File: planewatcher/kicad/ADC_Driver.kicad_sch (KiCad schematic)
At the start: 24 parts, among them U10 AD8138, U3 OPA2320

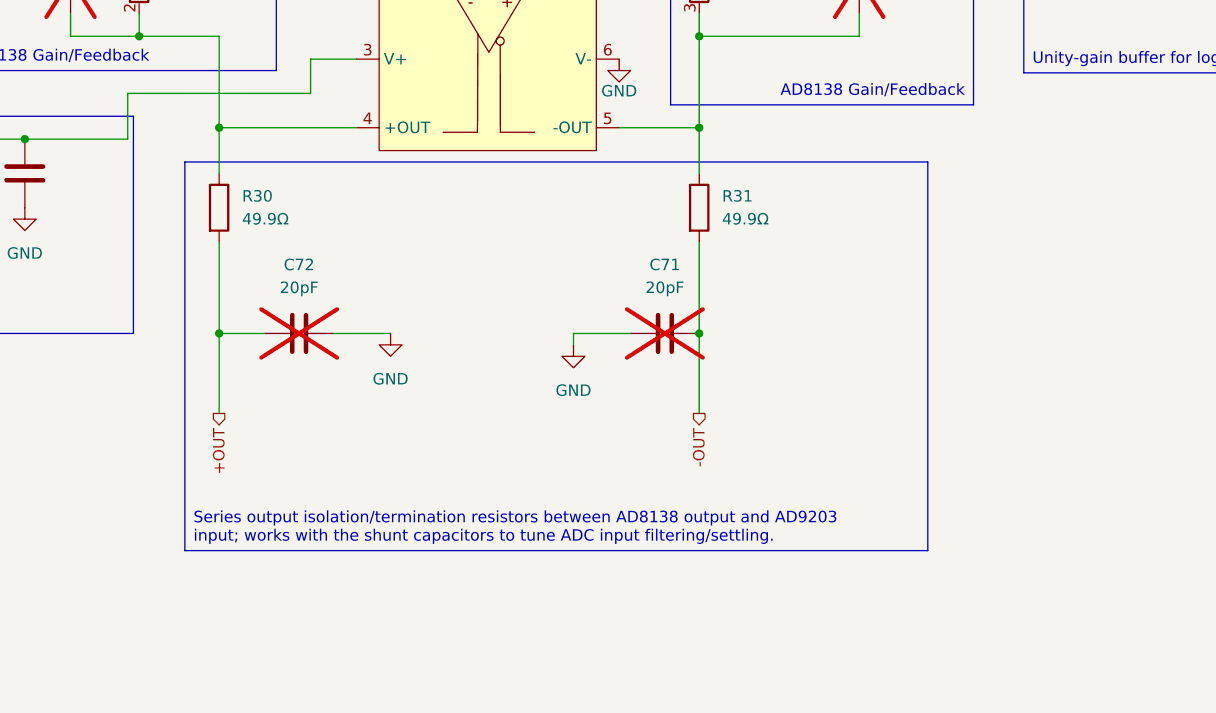
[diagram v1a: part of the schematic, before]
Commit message: Add RF pi matching networks + more
- Remove EEPROM write project solder jumper
- Update proto 1.3 documentation
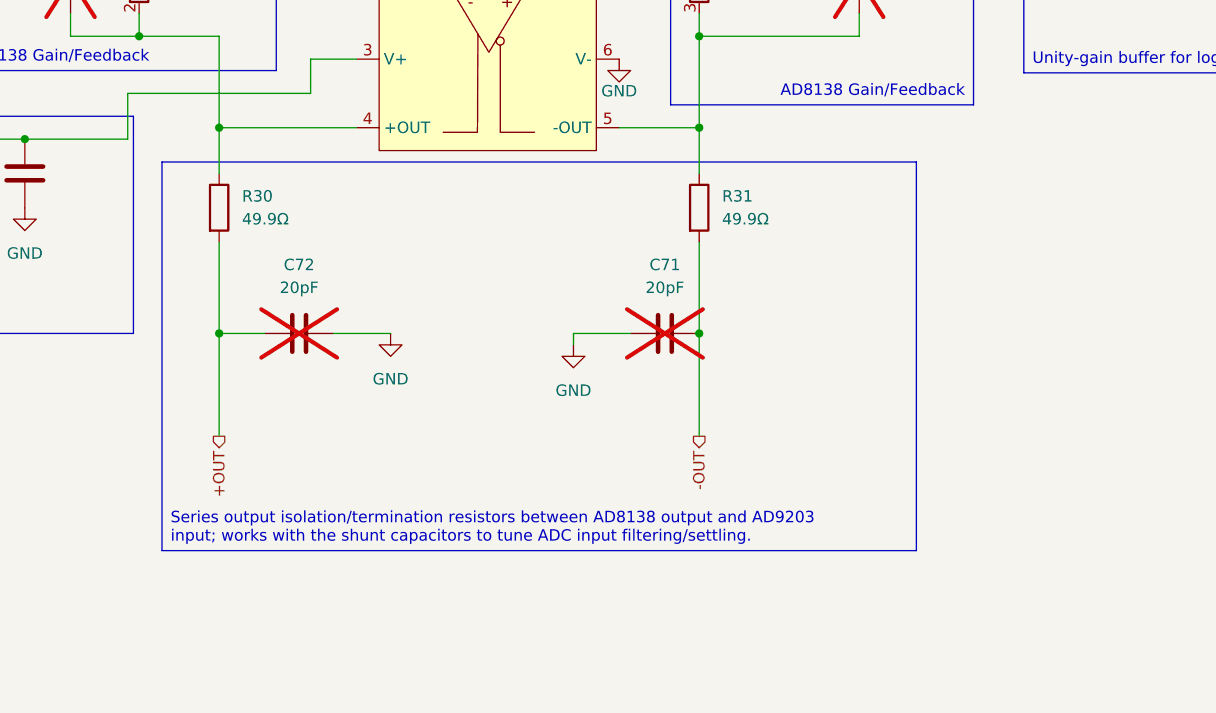
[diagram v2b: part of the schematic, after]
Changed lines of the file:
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@@
 	(text_box "Series output isolation/termination resistors between AD8138 output and AD9203 input; works with the shunt capacitors to tune ADC input filtering/settling."
 		(exclude_from_sim no)
-		(at 114.3 119.38 0)
-		(size 82.55 43.18)
+		(at 111.76 119.38 0)
+		(size 83.82 43.18)
 		(margins 0.9525 0.9525 0.9525 0.9525)
 		(stroke
@@
 	)
 	(junction
+		(at 109.22 105.41)
+		(diameter 0)
+		(color 0 0 0 0)
+	)
+	(junction
 		(at 118.11 138.43)
 		(diameter 0)
@@
 	)
 	(junction
-		(at 109.22 105.41)
+		(at 171.45 138.43)
 		(diameter 0)
 		(color 0 0 0 0)
@@
 	(junction
 		(at 220.98 74.93)
-		(diameter 0)
-		(color 0 0 0 0)
-	)
-	(junction
-		(at 171.45 138.43)
 		(diameter 0)
 		(color 0 0 0 0)
@@
 	(wire
 		(pts
-			(xy 171.45 138.43) (xy 171.45 147.32)
+			(xy 171.45 138.43) (xy 171.45 149.86)
 		)
 		(stroke
@@
 	(wire
 		(pts
-			(xy 118.11 138.43) (xy 118.11 147.32)
+			(xy 118.11 138.43) (xy 118.11 149.86)
 		)
 		(stroke
@@
 	(hierarchical_label "-OUT"
 		(shape output)
-		(at 171.45 147.32 270)
+		(at 171.45 149.86 270)
 		(effects
 			(font
@@
 	(hierarchical_label "+OUT"
 		(shape output)
-		(at 118.11 147.32 270)
+		(at 118.11 149.86 270)
 		(effects
 			(font
@@
 		)
 	)
+	(netclass_flag ""
+		(length 2.54)
+		(shape round)
+		(at 118.11 147.32 90)
+		(fields_autoplaced yes)
+		(effects
+			(font
+				(size 1.27 1.27)
+			)
+			(justify left bottom)
+		)
+		(property "Netclass" "DIFFPAIR_100Ω"
+			(at 115.57 146.6215 90)
+			(show_name no)
+			(do_not_autoplace no)
+			(effects
+				(font
+					(size 1.27 1.27)
+				)
+				(justify left)
+			)
+		)
+		(property "Component Class" ""
+			(at -85.09 10.16 0)
+			(show_name no)
+			(do_not_autoplace no)
+			(effects
+				(font
+					(size 1.27 1.27)
+					(italic yes)
+				)
+			)
+		)
+	)
+	(netclass_flag ""
+		(length 2.54)
+		(shape round)
+		(at 171.45 147.32 270)
+		(fields_autoplaced yes)
+		(effects
+			(font
+				(size 1.27 1.27)
+			)
+			(justify right bottom)
+		)
+		(property "Netclass" "DIFFPAIR_100Ω"
+			(at 173.99 146.6215 90)
+			(show_name no)
+			(do_not_autoplace no)
+			(effects
+				(font
+					(size 1.27 1.27)
+				)
+				(justify left)
+			)
+		)
+		(property "Component Class" ""
+			(at -31.75 10.16 0)
+			(show_name no)
+			(do_not_autoplace no)
+			(effects
+				(font
+					(size 1.27 1.27)
+					(italic yes)
+				)
+			)
+		)
+	)

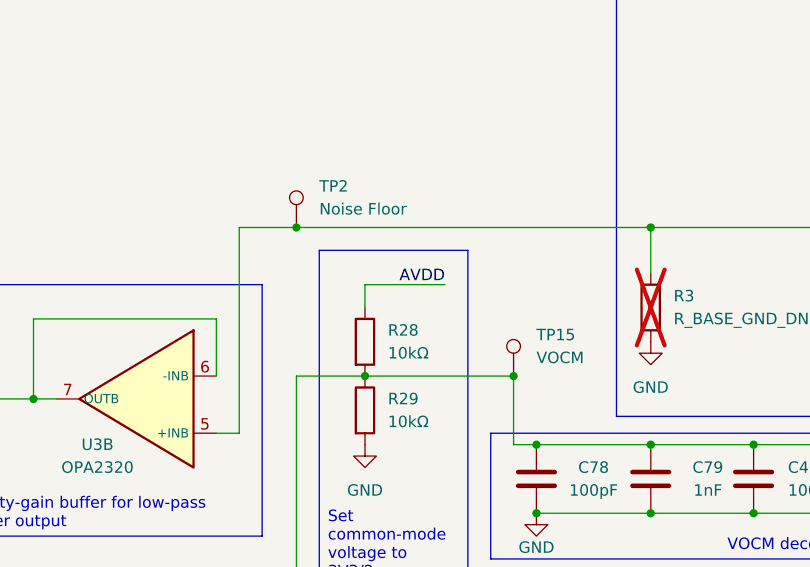
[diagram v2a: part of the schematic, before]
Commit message: Change LCSC column name, add fabrication toolkit options
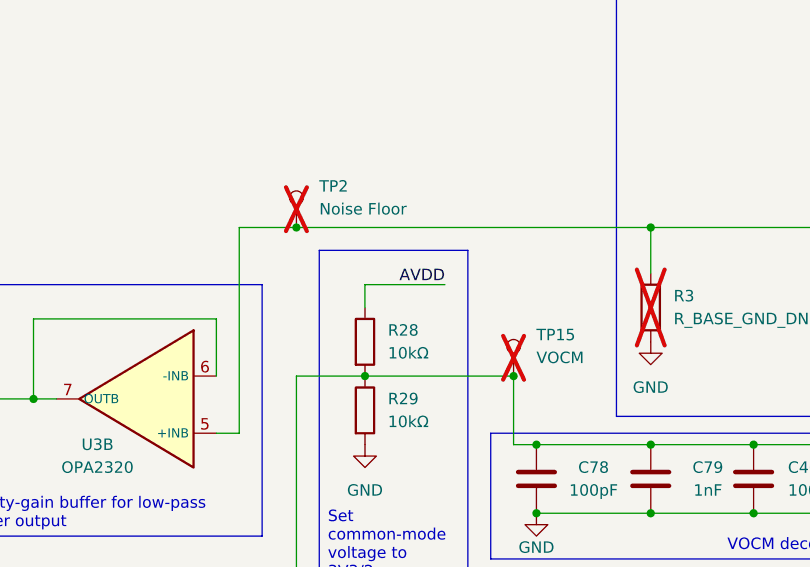
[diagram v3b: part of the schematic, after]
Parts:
- C46, C48, C65: LCSC (none) -> C161163; lcsc_id C161163 -> (none)
- C47, C64, C80: LCSC (none) -> C237435; lcsc_id C237435 -> (none)
- C71, C72: LCSC (none) -> C913479; lcsc_id C913479 -> (none)
- C78: LCSC (none) -> C2941926; lcsc_id C2941926 -> (none)
- C79: LCSC (none) -> C126493; lcsc_id C126493 -> (none)
- C9: LCSC (none) -> C5362585; lcsc_id C5362585 -> (none)
- R28, R29: LCSC (none) -> C191915; lcsc_id C191915 -> (none)
- R3: LCSC (none) -> C242160; lcsc_id C242160 -> (none)
- R30, R31: LCSC (none) -> C852809; lcsc_id C852809 -> (none)
- R51: LCSC (none) -> C413126; lcsc_id C413126 -> (none)
- RN1: LCSC (none) -> C620896; lcsc_id C620896 -> (none)
- TP15, TP2: now not fitted
- U10: LCSC (none) -> C113762; lcsc_id C113762 -> (none)
- U3: LCSC (none) -> C2057346; lcsc_id C2057346 -> (none)
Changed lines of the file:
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@@
 			(justify left bottom)
 		)
-		(property "Netclass" "DIFFPAIR_100Ω"
+		(property "Net Class" "DIFFPAIR_100Ω"
 			(at 115.57 146.6215 90)
 			(show_name no)
@@
 			(justify right bottom)
 		)
-		(property "Netclass" "DIFFPAIR_100Ω"
+		(property "Net Class" "DIFFPAIR_100Ω"
 			(at 173.99 146.6215 90)
 			(show_name no)
@@
 			)
 		)
-		(property "lcsc_id" "C852809"
+		(property "LCSC" "C852809"
 			(at 118.11 124.46 0)
 			(hide yes)
@@
 			)
 		)
-		(property "lcsc_id" "C237435"
+		(property "LCSC" "C237435"
 			(at 191.77 69.85 0)
 			(hide yes)
@@
 			)
 		)
-		(property "lcsc_id" "C2941926"
+		(property "LCSC" "C2941926"
 			(at 154.94 69.85 0)
 			(hide yes)
@@
 			)
 		)
-		(property "lcsc_id" "C126493"
+		(property "LCSC" "C126493"
 			(at 167.64 69.85 0)
 			(hide yes)
@@
 			)
 		)
-		(property "lcsc_id" "C620896"
+		(property "LCSC" "C620896"
 			(at 109.22 99.06 0)
 			(hide yes)
@@
 			)
 		)
-		(property "lcsc_id" "C852809"
+		(property "LCSC" "C852809"
 			(at 171.45 124.46 0)
 			(hide yes)
@@
 			)
 		)
-		(property "lcsc_id" "C2057346"
+		(property "LCSC" "C2057346"
 			(at 111.76 45.72 0)
 			(hide yes)
@@
 			)
 		)
-		(property "lcsc_id" "C620896"
+		(property "LCSC" "C620896"
 			(at 95.25 92.71 90)
 			(hide yes)
@@
 			)
 		)
-		(property "lcsc_id" "C161163"
+		(property "LCSC" "C161163"
 			(at 179.07 69.85 0)
 			(hide yes)
@@
 			)
 		)
-		(property "lcsc_id" "C620896"
+		(property "LCSC" "C620896"
 			(at 193.04 92.71 90)
 			(hide yes)
@@
 			)
 		)
-		(property "lcsc_id" "C113762"
+		(property "LCSC" "C113762"
 			(at 147.32 87.63 0)
 			(hide yes)
@@
 		(on_board yes)
 		(in_pos_files yes)
-		(dnp no)
+		(dnp yes)
 		(fields_autoplaced yes)
 		(property "Reference" "TP2"
@@
 			)
 		)
-		(property "lcsc_id" "C5362585"
+		(property "LCSC" "C5362585"
 			(at 191.77 50.8 0)
 			(hide yes)
@@
 			)
 		)
-		(property "lcsc_id" "C913479"
+		(property "LCSC" "C913479"
 			(at 167.64 138.43 90)
 			(hide yes)
@@
 			)
 		)
-		(property "lcsc_id" "C2057346"
+		(property "LCSC" "C2057346"
 			(at 243.84 77.47 0)
 			(hide yes)
@@
 			)
 		)
-		(property "lcsc_id" "C161163"
+		(property "LCSC" "C161163"
 			(at 234.95 78.74 0)
 			(hide yes)
@@
 			)
 		)
-		(property "lcsc_id" "C620896"
+		(property "LCSC" "C620896"
 			(at 171.45 99.06 0)
 			(hide yes)
@@
 		(on_board yes)
 		(in_pos_files yes)
-		(dnp no)
+		(dnp yes)
 		(fields_autoplaced yes)
 		(property "Reference" "TP15"
@@
 			)
 		)
-		(property "lcsc_id" "C191915"
+		(property "LCSC" "C191915"
 			(at 135.89 62.23 0)
 			(hide yes)
@@
 			)
 		)
-		(property "lcsc_id" "C242160"
+		(property "LCSC" "C242160"
 			(at 167.64 50.8 0)
 			(hide yes)
@@
 			)
 		)
-		(property "lcsc_id" "C413126"
+		(property "LCSC" "C413126"
 			(at 198.12 41.91 90)
 			(hide yes)
@@
 			)
 		)
-		(property "lcsc_id" "C161163"
+		(property "LCSC" "C161163"
 			(at 96.52 120.65 0)
 			(hide yes)
@@
 			)
 		)
-		(property "lcsc_id" "C237435"
+		(property "LCSC" "C237435"
 			(at 82.55 120.65 0)
 			(hide yes)
@@
 			)
 		)
-		(property "lcsc_id" "C237435"
+		(property "LCSC" "C237435"
 			(at 220.98 78.74 0)
 			(hide yes)
@@
 			)
 		)
-		(property "lcsc_id" "C913479"
+		(property "LCSC" "C913479"
 			(at 127 138.43 90)
 			(hide yes)
@@
 			)
 		)
-		(property "lcsc_id" "C191915"
+		(property "LCSC" "C191915"
 			(at 135.89 54.61 0)
 			(hide yes)

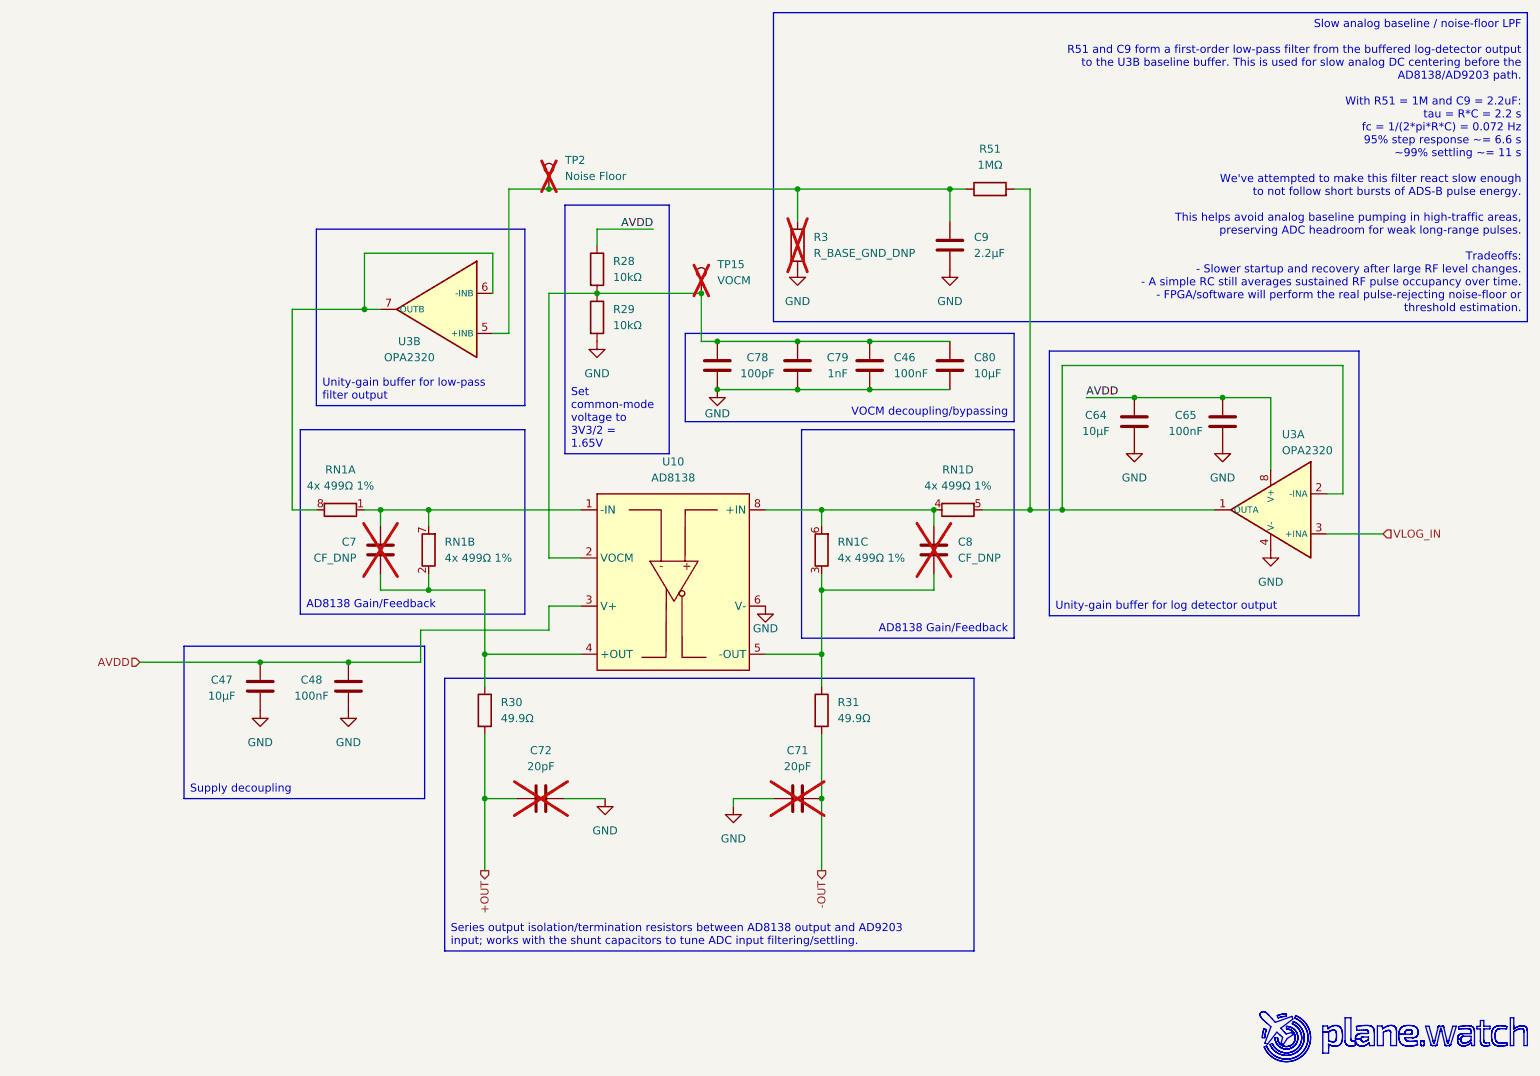
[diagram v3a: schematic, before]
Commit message: feat(planewatcher): revise rev 1.3 ADC buffer stages
- replace the OPA2320 with separate ADA4807-1 and OPA320 buffers
- update schematics, symbols, PCB placement, and routing
- refresh the op-amp datasheets
- document the new buffer architecture and update the board render
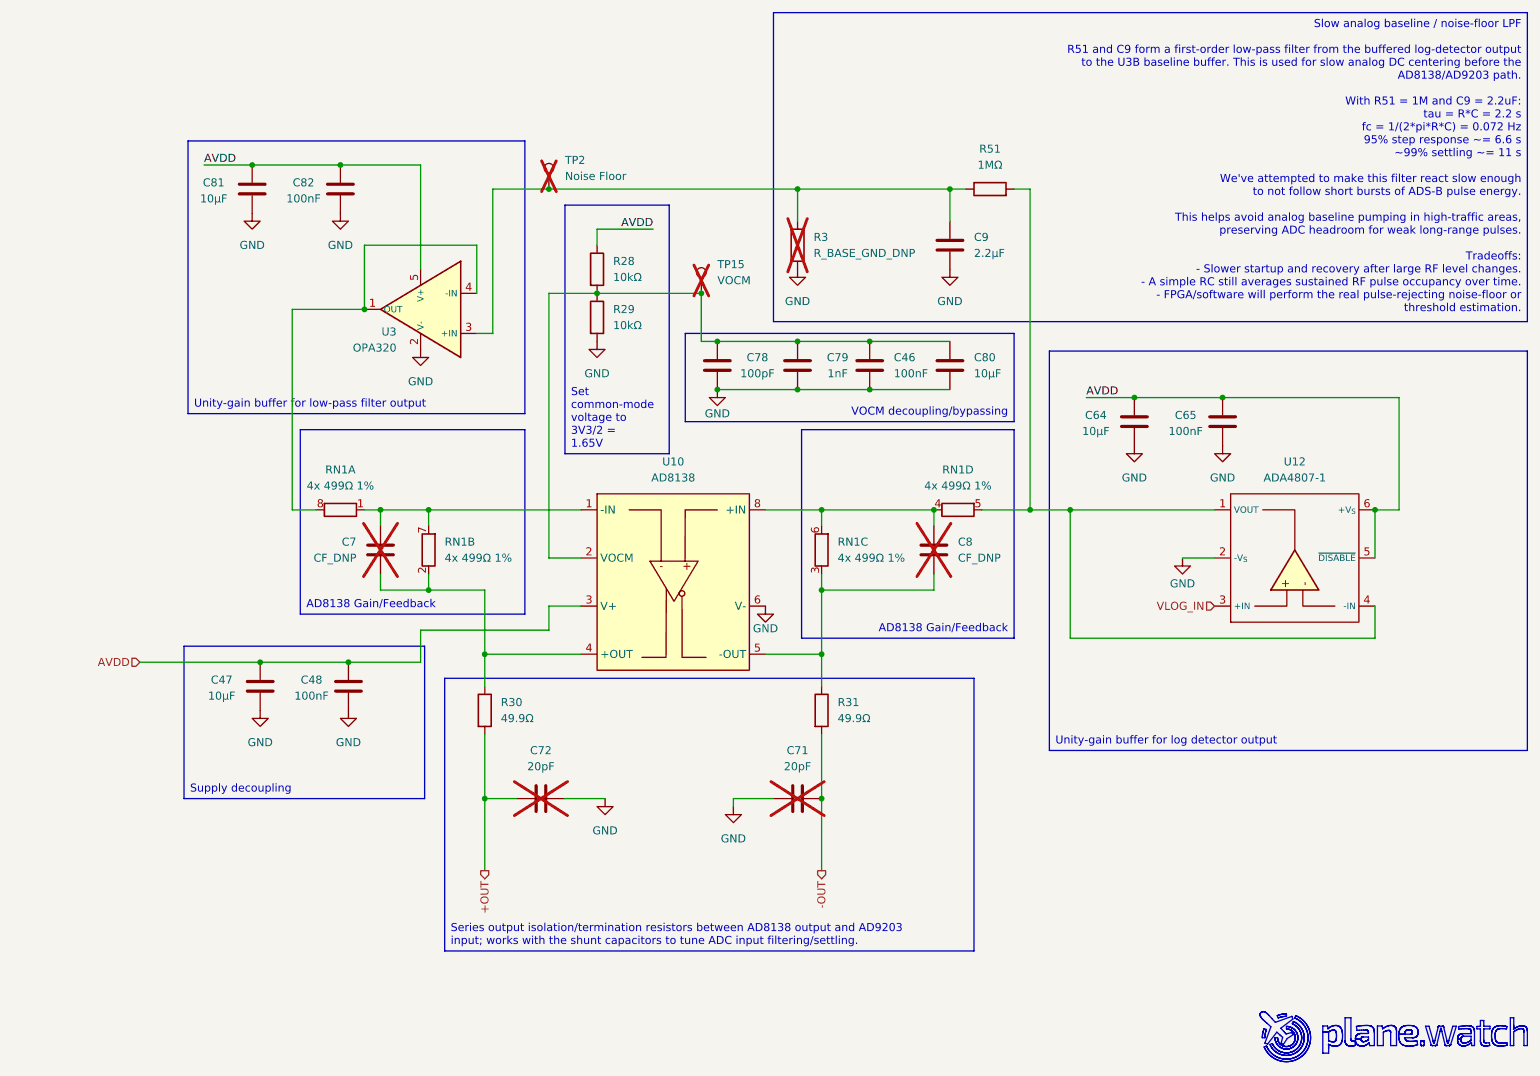
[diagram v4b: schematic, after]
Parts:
- removed U3: OPA2320, planewatcher:OPA2320 DRG0008A, symbol planewatcher:OPA2320
- added C81: 10µF, Capacitor_SMD:C_0603_1608Metric, symbol Device:C
- added C82: 100nF, Capacitor_SMD:C_0402_1005Metric, symbol Device:C
- added U12: ADA4807-1, Package_TO_SOT_SMD:SOT-23-6, symbol planewatcher:ADA4807-1
- added U3: OPA320, Package_TO_SOT_SMD:SOT-23-5, symbol planewatcher:OPA320
- C64: Purpose Local bulk decoupling for the OPA2320. -> Local bulk decoupling for ADA4807-1.
- C65: Purpose Local high-frequency decoupling for the OPA2320 supply. -> Local high-frequency decoupling for the ADA4807-1 supply.
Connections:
- net AVDD: now also C81.1, C82.1, U12.5 (~{DISABLE}), U12.6 (+V_{S}), U3.5 (V+)
- net GND: now also C81.2, C82.2, U12.2 (-V_{S}), U3.2 (V-)
- net VLOG_IN: now also U12.3 (+IN)
- net at C9.1, R3.1, R51.1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: now also U3.3 (+IN)
- net at RN1.8 (R1.2): now also U3.1 (OUT), U3.4 (-IN)
- net at R51.2, RN1.5 (R4.2): now also U12.1 (VOUT), U12.4 (-IN)

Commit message: Adjust component grouping
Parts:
- C46, C48, C65, C82: value 100nF -> 0.1µF
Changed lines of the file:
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@@
 			)
 		)
-		(property "Value" "100nF"
+		(property "Value" "0.1µF"
 			(at 89.408 43.434 0)
 			(show_name no)
@@
 			)
 		)
-		(property "Value" "100nF"
+		(property "Value" "0.1µF"
 			(at 182.88 71.1199 0)
 			(show_name no)
@@
 			)
 		)
-		(property "Value" "100nF"
+		(property "Value" "0.1µF"
 			(at 229.108 80.264 0)
 			(show_name no)
@@
 			)
 		)
-		(property "Value" "100nF"
+		(property "Value" "0.1µF"
 			(at 90.678 122.174 0)
 			(show_name no)
